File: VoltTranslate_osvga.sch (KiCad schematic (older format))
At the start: 4 parts, among them U1 SN74LVCH16T245DGGR, U2 SN74LVCH16T245DGGR, U3 SN74LVCH16T245DGGR, U4 SN74LVCH16T245DGGR

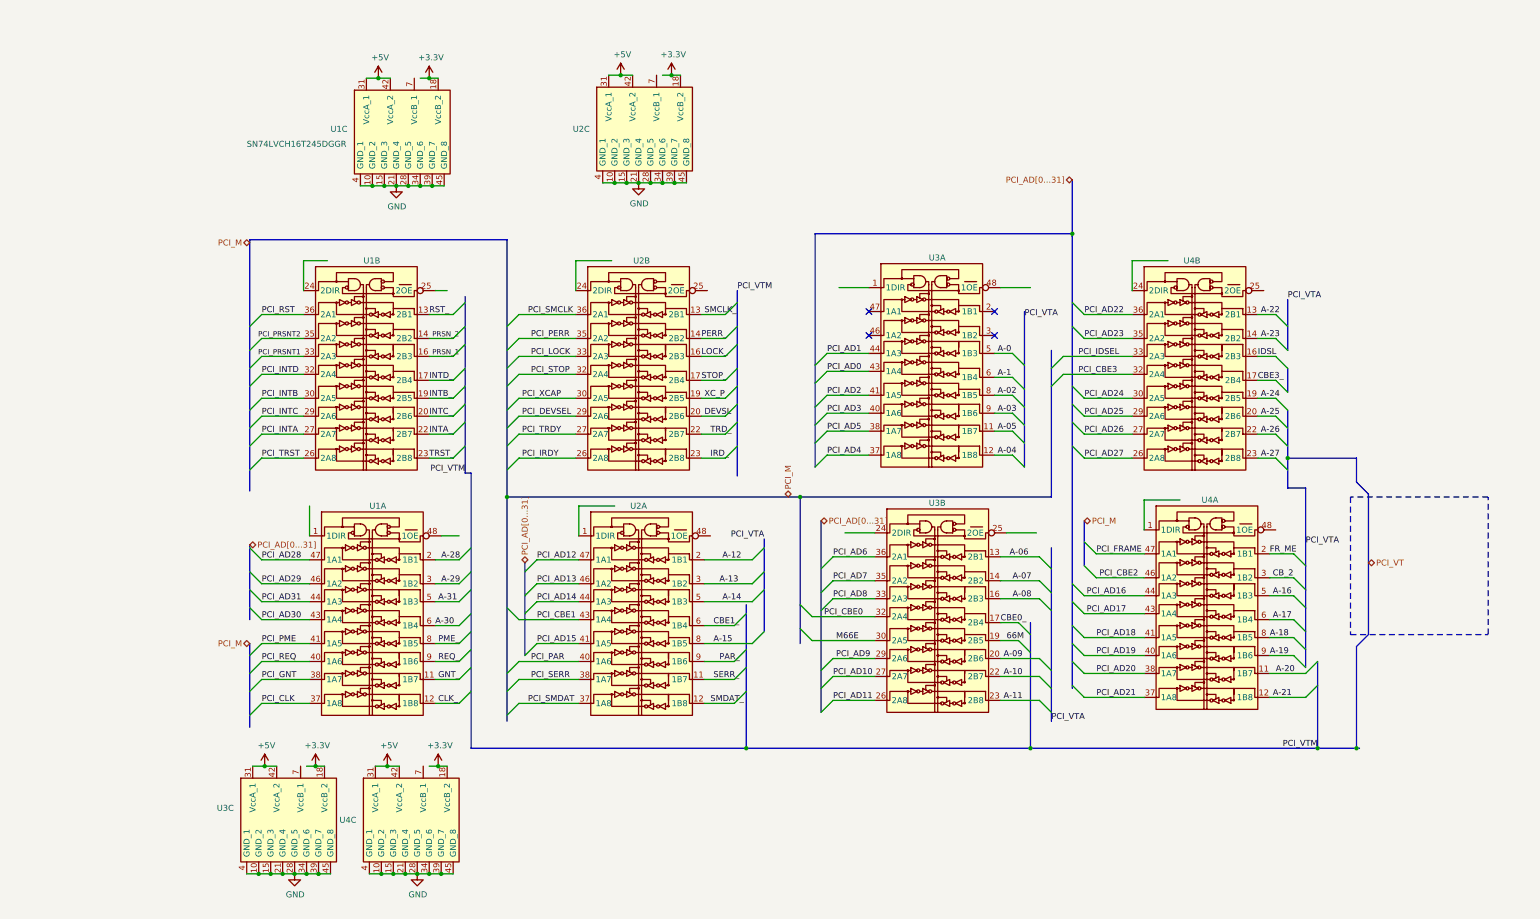
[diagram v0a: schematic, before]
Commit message: Add files via upload
Added Pull-up and pull-down resistors for JTAG and sysConfig connections.
Added pinheaders for FPGA-Configuration. (replacing edge-connector)
Combined the DVI+VGA and USB-C hierarchical sheets into one.
Assigned a dedicated sheet for the DAC.
Added 75 Ohm terminal-resistors to output of DAC.
Placed filtering-capacitors for DAC VAA.
Connected VGA ID-bits and DVI DDC together.
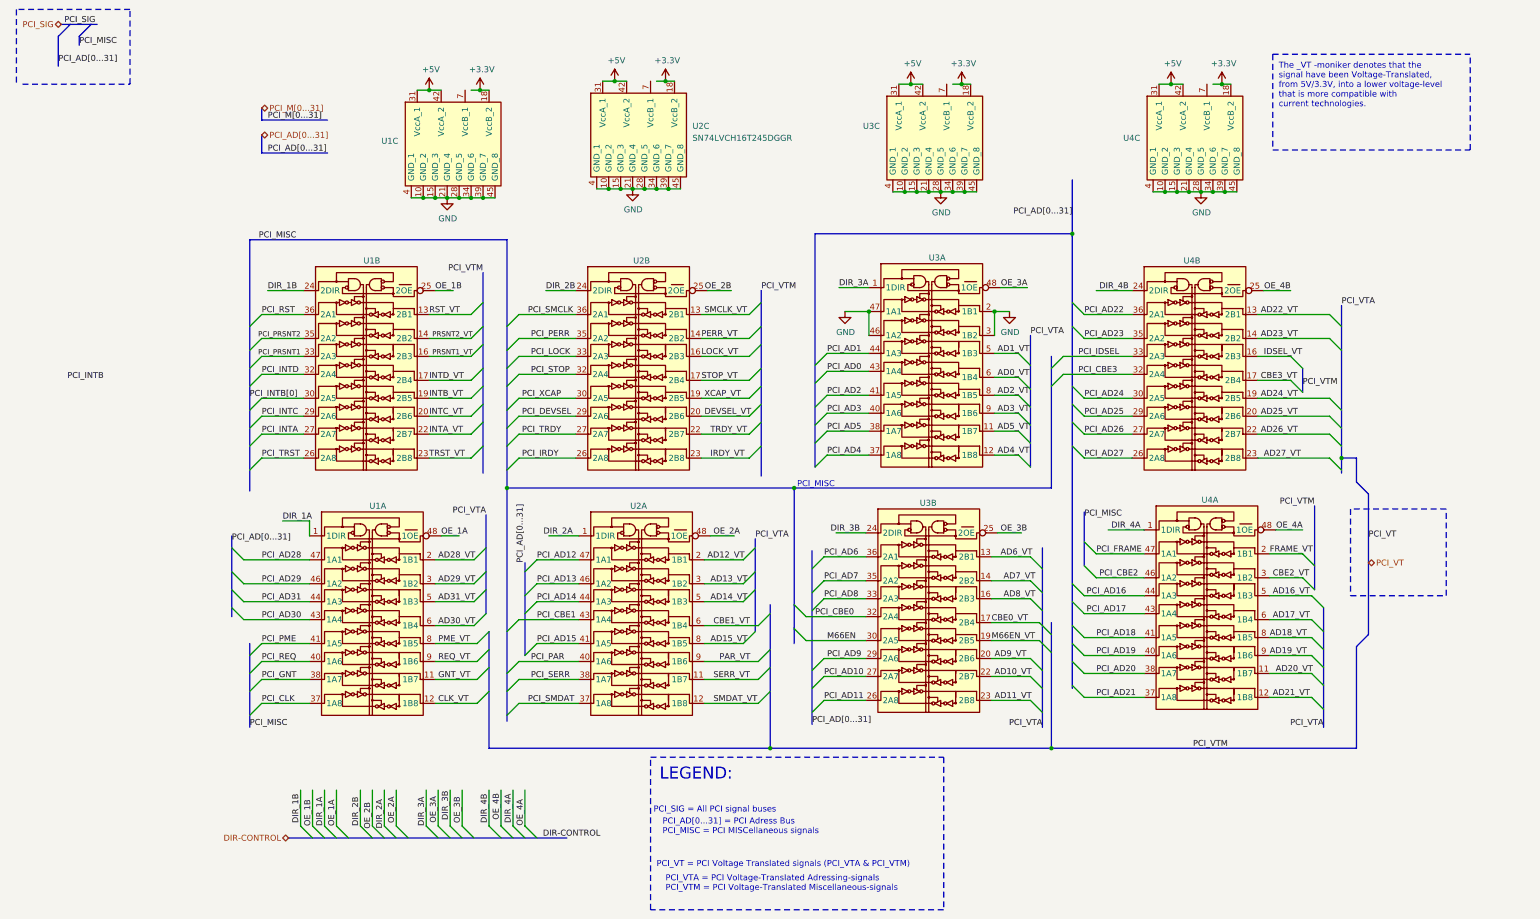
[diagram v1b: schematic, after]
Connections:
- net labels added: AD0_VT, AD10_VT, AD11_VT, AD12_VT, AD13_VT, AD14_VT, AD15_VT, AD16_VT, AD17_VT, AD18_VT, AD19_VT, AD1_VT, AD20_VT, AD21_VT, AD22_VT, AD23_VT, AD24_VT, AD25_VT, AD26_VT, AD27_VT, AD28_VT, AD29_VT, AD2_VT, AD30_VT, AD31_VT, AD3_VT, AD4_VT, AD5_VT, AD6_VT, AD7_VT, AD8_VT, AD9_VT, CBE0_VT, CBE1_VT, CBE2_VT, CBE3_VT, CLK_VT, DEVSEL_VT, DIR-CONTROL, DIR_1A, DIR_1B, DIR_2A, DIR_2B, DIR_3A, DIR_3B, DIR_4A, DIR_4B, FRAME_VT, GNT_VT, IDSEL_VT, INTA_VT, INTB_VT, INTC_VT, INTD_VT, IRDY_VT, LOCK_VT, M66EN, M66EN_VT, OE_1A, OE_1B, OE_2A, OE_2B, OE_3A, OE_3B, OE_4A, OE_4B, PAR_VT, PCI_INTB[0], PCI_MISC, PCI_M[0...31], PCI_SIG, PERR_VT, PME_VT, PRSNT1_VT, PRSNT2_VT, REQ_VT, RST_VT, SERR_VT, SMCLK_VT, SMDAT_VT, STOP_VT, TRDY_VT, TRST_VT, XCAP_VT
- net labels removed: 66M, A-0, A-02, A-03, A-04, A-05, A-06, A-07, A-08, A-09, A-1, A-10, A-11, A-12, A-13, A-14, A-15, A-16, A-17, A-18, A-19, A-20, A-21, A-22, A-23, A-24, A-25, A-26, A-27, A-28, A-29, A-30, A-31, CBE0_, CBE1_, CBE3_, CB_2, CLK_, DEVSL, FR_ME, GNT_, IDSL, INTA_, INTB_, INTC_, INTD_, IRD_, LOCK_, M66E, PAR_, PCI_M, PERR_, PME_, PRSN_1, PRSN_2, REQ_, RST_, SERR_, SMCLK_, SMDAT_, STOP_, TRD_, TRST_, XC_P
- wire segments 185 -> 205
- no-connect marks 4 -> 0
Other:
- note added: "LEGEND:"
- note added: "PCI_AD[0...31] = PCI Adress Bus\nPCI_MISC = PCI MISCellaneous signals"
- note added: "PCI_MISC"
- note added: "PCI_SIG = All PCI signal buses\n\n"
- note added: "PCI_VT = PCI Voltage Translated signals (PCI_VTA & PCI_VTM)"
- note added: "PCI_VTA = PCI Voltage-Translated Adressing-signals\nPCI_VTM = PCI Voltage-Translated Miscellaneous-signals"
- note added: "The _VT -moniker denotes that the \nsignal have been Voltage-Translated, \nfrom 5V/3.3V, into a lower voltage-level \nthat is more compatible with \ncurrent technologies."
- moved on the sheet: U1C, U2C, U3B, U3C, U4C

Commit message: Add files via upload
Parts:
- added C70, C71, C72, C73, C74, C75, C76, C77: C1206C105K4RACTU, Capacitor_SMD:C_1206_3216Metric_Pad1.42x1.75mm_HandSolder, symbol LRJ-parts:C1206C105K4RACTU
- added C80, C81, C82, C83, C84, C85, C86, C87, C90, C91, C92, C93, C94, C95, C96, C97: VJ1206Y104JXAAR, Capacitor_SMD:C_1206_3216Metric_Pad1.42x1.75mm_HandSolder, symbol LRJ-parts:VJ1206Y104JXAAR
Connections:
- net labels added: +1V2
- net labels removed: PCI_INTB[0], PCI_M[0...31]
- wire segments 205 -> 273
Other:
- moved on the sheet: U1C, U2C
